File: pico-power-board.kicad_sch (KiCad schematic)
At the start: 58 parts, among them J1 Conn_02x10_Counter_Clockwise, J10 Conn_01x07_Male, J2 Conn_02x10_Counter_Clockwise, J3 Conn_02x10_Counter_Clockwise, J4 Conn_02x10_Counter_Clockwise, J5 Conn_02x10_Counter_Clockwise, J6 Conn_02x10_Counter_Clockwise, J7 DC-053D-25A, J8 Conn_01x20_Female, J9 Conn_01x20_Female, U1 INA219AxD, U2 SN74HC541NSR, U3 K7803-500R3, U4 TMP102AIDRLR

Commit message: Update project for prototyping
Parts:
- F1, F2, F3, F4, F5, F6: LCSC C315895 -> C883135
- J1, J10, J2, J3, J4, J5, J6, J8, J9: JLC in-line,P=2.54mm -> Plugin,P=2.54mm
- J7, U3: JLC plug-in -> Plugin
- JP1, JP2: JLC (none) -> Plugin,P=2.54mm; LCSC (none) -> C2829889
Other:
- note added: "TODO: - DONE use different fuse (hold current of 2A instead of 1.5A) - e.g. LCSC: C883135 - DONE check shunt resistor current rating (1W rated resistor, reached at 10A = max. of 120W power supply) - check inner diameter of barrel jack (2.1 or 2.5mm) -> probably 2.5mm - DC Jack and Female Headers out of stock at JLCPCB - maybe pre-order those parts"
- note removed: "alternatives: - LMS78_03-0.5R from Gaptec - K7803-500R3 from Mornsun or Dexu"

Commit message: Implement improvements from review comments
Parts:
- removed R13, R18, R19, R20, R21, R22: 10k, Resistor_SMD:R_0603_1608Metric, symbol Device:R
- J10: value Conn_01x07_Male -> Conn_01x06_Male; footprint Connector_PinSocket_2.54mm:PinSocket_1x07_P2.54mm_Vertical -> Connector_PinHeader_2.54mm:PinHeader_1x06_P2.54mm_Vertical; symbol Connector:Conn_01x07_Male -> Connector:Conn_01x06_Pin; LCSC C492406 -> C2935912
- R17: value 10k -> 3.3k; LCSC C25804 -> C22978
- renumbered C2 to C1, C1 to C2, J7 to J4, J4 to J5, J5 to J6, J6 to J7, R9 to R10, R10 to R11, R11 to R12, R12 to R13, R15 to R14, R16 to R15, R23 to R16, R14 to R7, R7 to R8, R8 to R9, U4 to U3, U3 to U4
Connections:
- net +12V: now also R7.1, U1.8 (IN+); no longer R7.2, U1.7 (IN-)
- net +3V3: now also R17.1; no longer R17.2
- net 12V_IN: now also R7.2, U1.7 (IN-); no longer R7.1, U1.8 (IN+)
- net CS1: now also U2.17 (Y2); no longer U2.18 (Y1)
- net CS1_Pico: now also J8.4 (Pin_4), U2.3 (A2); no longer J8.20 (Pin_20), R17.1, U2.2 (A1)
- net CS2: now also U2.15 (Y4); no longer U2.17 (Y2)
- net CS2_Pico: now also J8.6 (Pin_6), U2.5 (A4); no longer J8.17 (Pin_17), JP1.2 (B), U2.3 (A2)
- net CS3_Pico: now also J8.9 (Pin_9); no longer J8.11 (Pin_11), JP2.2 (B)
- net CS4_Pico: now also J8.11 (Pin_11), JP2.2 (B); no longer J8.9 (Pin_9)
- net CS5_Pico: now also J8.17 (Pin_17), JP1.2 (B); no longer J8.6 (Pin_6)
- net CS6_Pico: now also J8.20 (Pin_20); no longer J8.4 (Pin_4)
- net MOSI: now also U2.18 (Y1); no longer U2.16 (Y3)
- net MOSI_Pico: now also U2.2 (A1); no longer U2.4 (A3)
- net SCK: now also U2.16 (Y3); no longer U2.15 (Y4)
- net SCK_Pico: now also U2.4 (A3); no longer U2.5 (A4)
- net UART0_RX: now also J10.6 (Pin_6); no longer J10.7 (Pin_7)
- net UART0_TX: now also J10.5 (Pin_5); no longer J10.6 (Pin_6)
- net ADC0/I2C_SDA renamed I2C_SDA
- net I2C_SDA: now also J10.3 (Pin_3); no longer J10.4 (Pin_4)
- net ADC1/I2C_SCL renamed I2C_SCL
- net I2C_SCL: now also J10.4 (Pin_4); no longer J10.5 (Pin_5)
- net ADC2 renamed ALERT
- net ALERT: now also R17.2; no longer J10.3 (Pin_3)
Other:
- note added: "Note: Inverted wiring to INA219 for easier routing (invert current measurement in software)"
- moved on the sheet: C3, C5, R15, R16

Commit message: Progress, I guess
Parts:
- removed JP1, JP2: Jumper_2_Open, Connector_PinHeader_2.54mm:PinHeader_1x02_P2.54mm_Vertical, symbol Jumper:Jumper_2_Open
- J8, J9: LCSC C50984 -> C429947
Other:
- note removed: "SCL"
- note removed: "SDA"
- note removed: "SPI alternative: I2C to Lamps"
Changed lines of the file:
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@@
     (effects (font (size 1.27 1.27)) (justify left bottom))
   )
-  (text "SDA" (at 144.018 110.998 0)
-    (effects (font (size 1.27 1.27)) (justify left bottom))
-  )
   (text "Breakout Header (UART/I2C/ADC/GPIO)" (at 245.11 63.119 0)
     (effects (font (size 1.27 1.27)) (justify left bottom))
@@
     (effects (font (size 1.27 1.27)) (justify left bottom))
   )
-  (text "SPI alternative:\nI2C to Lamps" (at 128.524 93.853 0)
-    (effects (font (size 1.27 1.27)) (justify left bottom))
-  )
   (text "Lighthouse Lamp Connectors" (at 86.36 15.875 0)
     (effects (font (size 1.27 1.27)) (justify right bottom))
   )
-  (text "SCL" (at 144.272 100.965 0)
-    (effects (font (size 1.27 1.27)) (justify left bottom))
-  )
   (text "Power LED" (at 224.282 135.001 0)
     (effects (font (size 1.27 1.27)) (justify left bottom))
@@
     )
   )
-  (global_label "CS4_Pico" (shape input) (at 140.335 112.268 0) (fields_autoplaced)
-    (effects (font (size 1.27 1.27)) (justify left))
-    (property "Intersheetrefs" "${INTERSHEET_REFS}" (at 152.0098 112.268 0)
-      (effects (font (size 1.27 1.27)) (justify left) hide)
-    )
-  )
   (global_label "CS4" (shape output) (at 85.09 57.15 180) (fields_autoplaced)
     (effects (font (size 1.27 1.27)) (justify right))
@@
     )
   )
-  (global_label "CS5_Pico" (shape input) (at 140.335 102.108 0) (fields_autoplaced)
-    (effects (font (size 1.27 1.27)) (justify left))
-    (property "Intersheetrefs" "${INTERSHEET_REFS}" (at 152.0098 102.108 0)
-      (effects (font (size 1.27 1.27)) (justify left) hide)
-    )
-  )
   (global_label "CS1" (shape output) (at 36.83 57.15 180) (fields_autoplaced)
     (effects (font (size 1.27 1.27)) (justify right))
@@
     )
   )
-  (global_label "MOSI" (shape output) (at 130.175 112.268 180) (fields_autoplaced)
-    (effects (font (size 1.27 1.27)) (justify right))
-    (property "Intersheetrefs" "${INTERSHEET_REFS}" (at 123.1657 112.3474 0)
-      (effects (font (size 1.27 1.27)) (justify right) hide)
-    )
-  )
   (global_label "I2C_SDA" (shape input) (at 267.843 73.406 180) (fields_autoplaced)
     (effects (font (size 1.27 1.27)) (justify right))
@@
     )
   )
-  (global_label "SCK" (shape output) (at 130.175 102.108 180) (fields_autoplaced)
-    (effects (font (size 1.27 1.27)) (justify right))
-    (property "Intersheetrefs" "${INTERSHEET_REFS}" (at 124.0124 102.0286 0)
-      (effects (font (size 1.27 1.27)) (justify right) hide)
-    )
-  )
   (global_label "MOSI" (shape input) (at 191.135 126.619 270) (fields_autoplaced)
     (effects (font (size 1.27 1.27)) (justify right))
@@
       (effects (font (size 1.27 1.27)) hide)
     )
-    (property "Datasheet" "https://datasheet.lcsc.com/lcsc/1810312312_BOOMELE-Boom-Precision-Elec-C50984_C50984.pdf" (at 213.36 49.149 0)
+    (property "Datasheet" "" (at 213.36 49.149 0)
       (effects (font (size 1.27 1.27)) hide)
     )
@@
       (effects (font (size 1.27 1.27)) hide)
     )
-    (property "LCSC" "C50984" (at 213.36 49.149 0)
+    (property "LCSC" "C429947" (at 213.36 49.149 0)
       (effects (font (size 1.27 1.27)) hide)
     )
@@
       (effects (font (size 1.27 1.27)) hide)
     )
-    (property "Datasheet" "https://datasheet.lcsc.com/lcsc/1810312312_BOOMELE-Boom-Precision-Elec-C50984_C50984.pdf" (at 196.977 49.149 0)
+    (property "Datasheet" "" (at 196.977 49.149 0)
       (effects (font (size 1.27 1.27)) hide)
     )
@@
       (effects (font (size 1.27 1.27)) hide)
     )
-    (property "LCSC" "C50984" (at 196.977 49.149 0)
+    (property "LCSC" "C429947" (at 196.977 49.149 0)
       (effects (font (size 1.27 1.27)) hide)
     )
@@
     )
   )
-  (symbol (lib_id "Jumper:Jumper_2_Open") (at 135.255 102.108 0) (unit 1)
-    (in_bom yes) (on_board yes) (dnp no) (fields_autoplaced)
-    (property "Reference" "JP1" (at 135.255 95.25 0)
-      (effects (font (size 1.27 1.27)))
-    )
-    (property "Value" "Jumper_2_Open" (at 135.255 97.79 0)
-      (effects (font (size 1.27 1.27)))
-    )
-    (property "Footprint" "Connector_PinHeader_2.54mm:PinHeader_1x02_P2.54mm_Vertical" (at 135.255 102.108 0)
-      (effects (font (size 1.27 1.27)) hide)
-    )
-    (property "Datasheet" "https://datasheet.lcsc.com/lcsc/2105241721_Liansheng-PH-00013_C2829889.pdf" (at 135.255 102.108 0)
-      (effects (font (size 1.27 1.27)) hide)
-    )
-    (property "JLC" "Plugin,P=2.54mm" (at 135.255 102.108 0)
-      (effects (font (size 1.27 1.27)) hide)
-    )
-    (property "LCSC" "C2829889" (at 135.255 102.108 0)
-      (effects (font (size 1.27 1.27)) hide)
-    )
-    (pin "1")
-    (pin "2")
-    (instances
-      (project "pico-power-board"
-        (path "/5bc25f0e-b3e0-4374-ab09-b14788ee45d5"
-          (reference "JP1") (unit 1)
-        )
-      )
-    )
-  )
   (symbol (lib_id "power:GND") (at 28.575 41.91 0) (unit 1)
     (in_bom yes) (on_board yes) (dnp no)
@@
         )
       )
-    )
-  )
-  (symbol (lib_id "Jumper:Jumper_2_Open") (at 135.255 112.268 0) (unit 1)
-    (in_bom yes) (on_board yes) (dnp no) (fields_autoplaced)
-    (property "Reference" "JP2" (at 135.255 105.537 0)
-      (effects (font (size 1.27 1.27)))
-    )
-    (property "Value" "Jumper_2_Open" (at 135.255 108.077 0)
-      (effects (font (size 1.27 1.27)))
-    )
-    (property "Footprint" "Connector_PinHeader_2.54mm:PinHeader_1x02_P2.54mm_Vertical" (at 135.255 112.268 0)
-      (effects (font (size 1.27 1.27)) hide)
-    )
-    (property "Datasheet" "https://datasheet.lcsc.com/lcsc/2105241721_Liansheng-PH-00013_C2829889.pdf" (at 135.255 112.268 0)
-      (effects (font (size 1.27 1.27)) hide)
-    )
-    (property "JLC" "Plugin,P=2.54mm" (at 135.255 112.268 0)
-      (effects (font (size 1.27 1.27)) hide)
-    )
-    (property "LCSC" "C2829889" (at 135.255 112.268 0)
-      (effects (font (size 1.27 1.27)) hide)
-    )
-    (pin "1")
-    (pin "2")
-    (instances
-      (project "pico-power-board"
-        (path "/5bc25f0e-b3e0-4374-ab09-b14788ee45d5"
-          (reference "JP2") (unit 1)
-        )
-      )

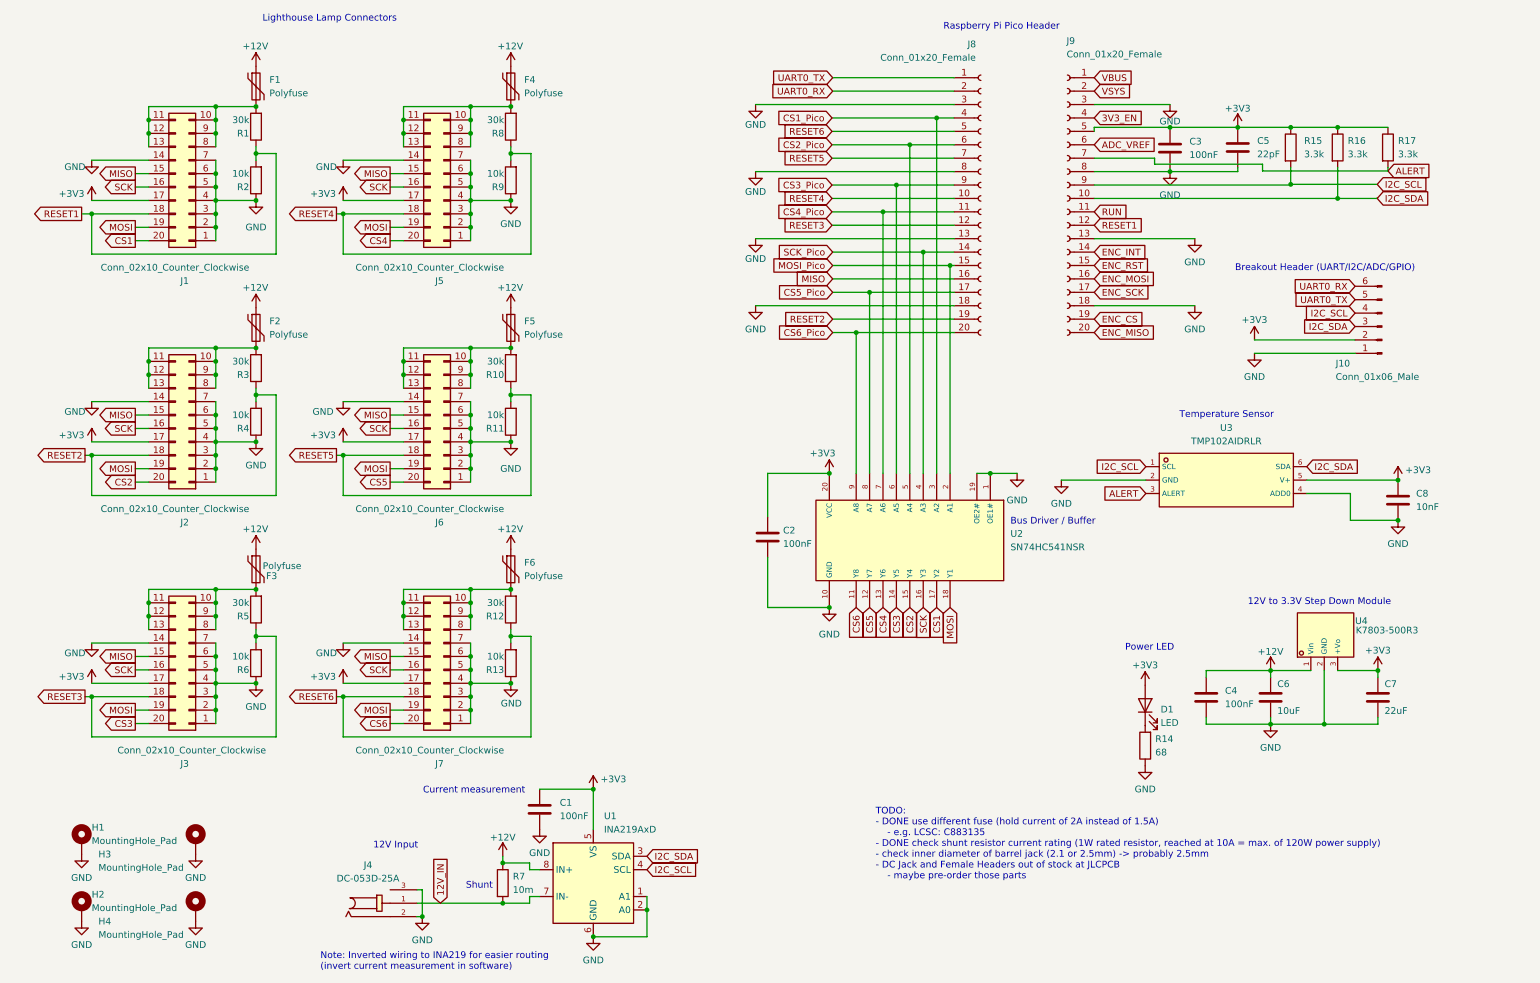
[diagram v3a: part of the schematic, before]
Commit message: Add SPI signal termination and remove line driver
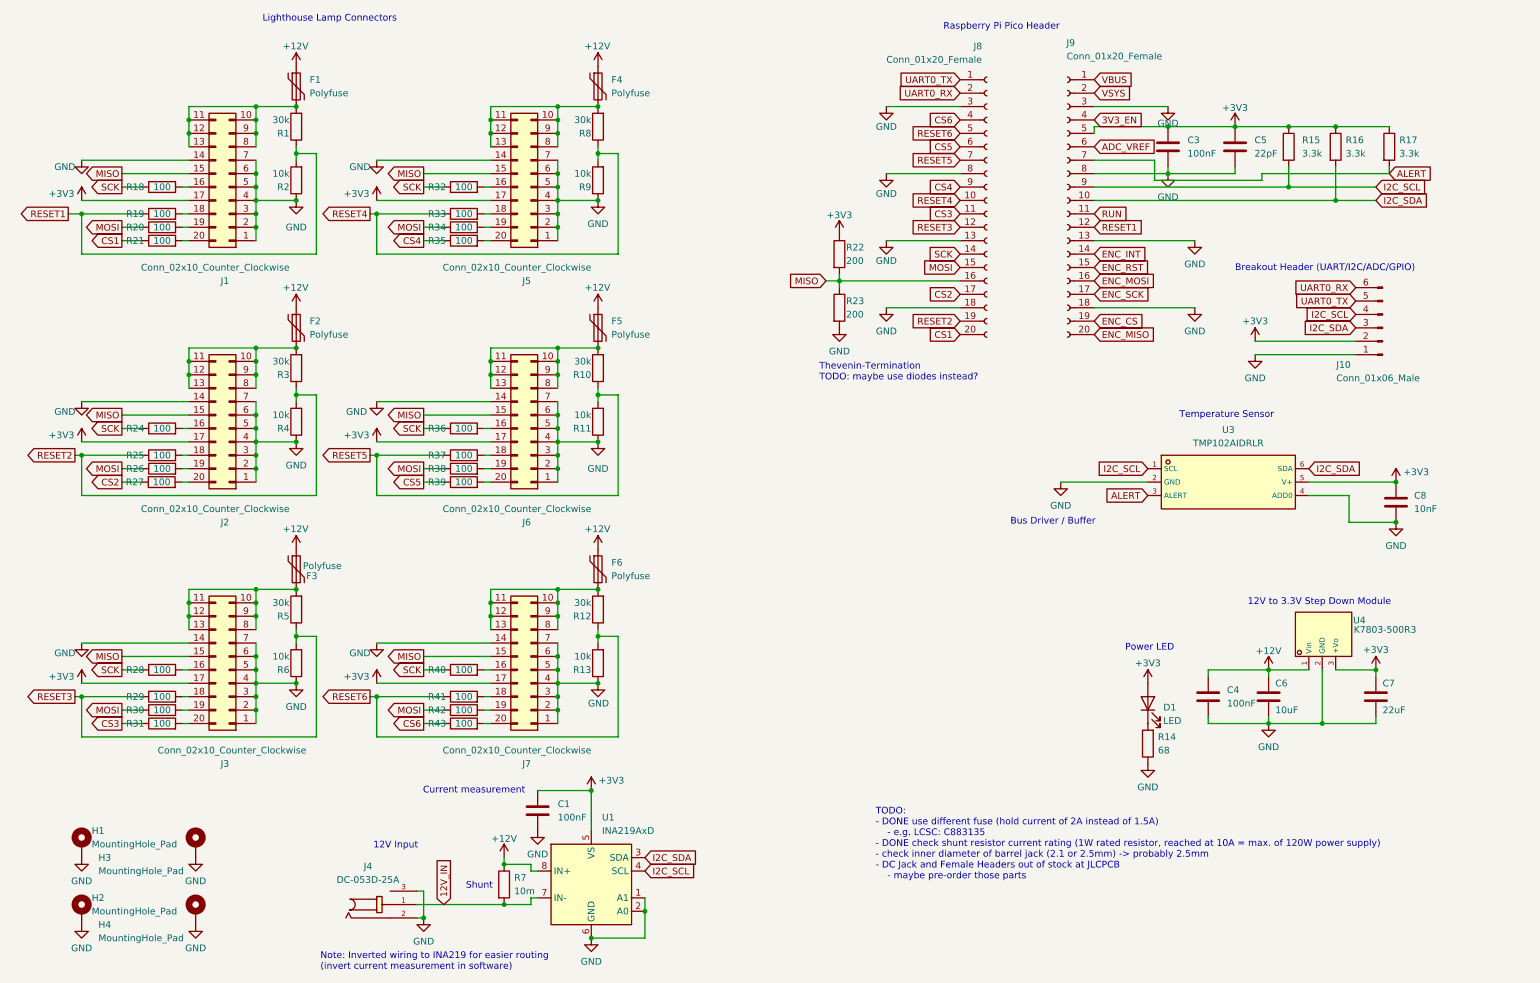
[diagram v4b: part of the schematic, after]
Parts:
- removed C2: 100nF, Capacitor_SMD:C_0603_1608Metric, symbol Device:C
- removed U2: SN74HC541NSR, Lighthouse:SOIC-20_L12.6-W5.3-P1.27-LS7.8-BL, symbol SN74HC541NSR_lib:SN74HC541NSR
- added R18, R19, R20, R21, R24, R25, R26, R27, R28, R29, R30, R31, R32, R33, R34, R35, R36, R37, R38, R39, R40, R41, R42, R43: 100, Resistor_SMD:R_0603_1608Metric, symbol Device:R
- added R22, R23: 200, Resistor_SMD:R_0603_1608Metric, symbol Device:R
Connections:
- net CS1_Pico is gone; now on net CS6: J8.4 (Pin_4)
- net CS2_Pico is gone; now on net CS5: J8.6 (Pin_6)
- net CS3_Pico is gone; now on net CS4: J8.9 (Pin_9)
- net CS4_Pico is gone; now on net CS3: J8.11 (Pin_11)
- net CS5_Pico is gone; now on net CS2: J8.17 (Pin_17)
- net CS6_Pico is gone; now on net CS1: J8.20 (Pin_20)
- net MOSI_Pico is gone; now on net MOSI: J8.15 (Pin_15)
- net SCK_Pico is gone; now on net SCK: J8.14 (Pin_14)
- net +3V3: now also R22.1
- net CS1: now also R21.1; no longer J1.20 (Pin_20)
- net CS2: now also R27.1; no longer J2.20 (Pin_20)
- net CS3: now also R31.1; no longer J3.20 (Pin_20)
- net CS4: now also R35.1; no longer J5.20 (Pin_20)
- net CS5: now also R39.1; no longer J6.20 (Pin_20)
- net CS6: now also R43.1; no longer J7.20 (Pin_20)
- net GND: now also R23.2
- net MISO: now also R22.2, R23.1
- net MOSI: now also R20.1, R26.1, R30.1, R34.1, R38.1, R42.1; no longer J1.19 (Pin_19), J2.19 (Pin_19), J3.19 (Pin_19), J5.19 (Pin_19), J6.19 (Pin_19), J7.19 (Pin_19)
- net RESET1: now also R19.1; no longer J1.18 (Pin_18)
- net RESET2: now also R25.1; no longer J2.18 (Pin_18)
- net RESET3: now also R29.1; no longer J3.18 (Pin_18)
- net RESET4: now also R33.1; no longer J5.18 (Pin_18)
- net RESET5: now also R37.1; no longer J6.18 (Pin_18)
- net RESET6: now also R41.1; no longer J7.18 (Pin_18)
- net SCK: now also R18.1, R24.1, R28.1, R32.1, R36.1, R40.1; no longer J1.16 (Pin_16), J2.16 (Pin_16), J3.16 (Pin_16), J5.16 (Pin_16), J6.16 (Pin_16), J7.16 (Pin_16)
- new net: J6.18 (Pin_18), R37.2
- new net: J2.16 (Pin_16), R24.2
- new net: J1.20 (Pin_20), R21.2
- new net: J1.18 (Pin_18), R19.2
- new net: J2.18 (Pin_18), R25.2
- new net: J7.16 (Pin_16), R40.2
- new net: J7.20 (Pin_20), R43.2
- new net: J3.16 (Pin_16), R28.2
- new net: J3.18 (Pin_18), R29.2
- new net: J3.19 (Pin_19), R30.2
- new net: J3.20 (Pin_20), R31.2
- new net: J1.16 (Pin_16), R18.2
- new net: J1.19 (Pin_19), R20.2
- new net: J5.18 (Pin_18), R33.2
- new net: J7.18 (Pin_18), R41.2
- new net: J5.16 (Pin_16), R32.2
- new net: J5.20 (Pin_20), R35.2
- new net: J6.19 (Pin_19), R38.2
- new net: J2.19 (Pin_19), R26.2
- new net: J2.20 (Pin_20), R27.2
- new net: J7.19 (Pin_19), R42.2
- new net: J5.19 (Pin_19), R34.2
- new net: J6.16 (Pin_16), R36.2
- new net: J6.20 (Pin_20), R39.2
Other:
- note added: "Thevenin-Termination TODO: maybe use diodes instead?"
- moved on the sheet: C5, C8, D1, F1, F2, F3, F4, F5, F6, H1, H2, H3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
